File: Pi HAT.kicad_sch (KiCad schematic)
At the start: 13 parts, among them J1 Screw_Terminal_01x04, J2 Screw_Terminal_01x04, J3 Screw_Terminal_01x04, J5 Screw_Terminal_01x03, J6 Screw_Terminal_01x03, J7 GPIO_CONNECTOR, Q1 S8550

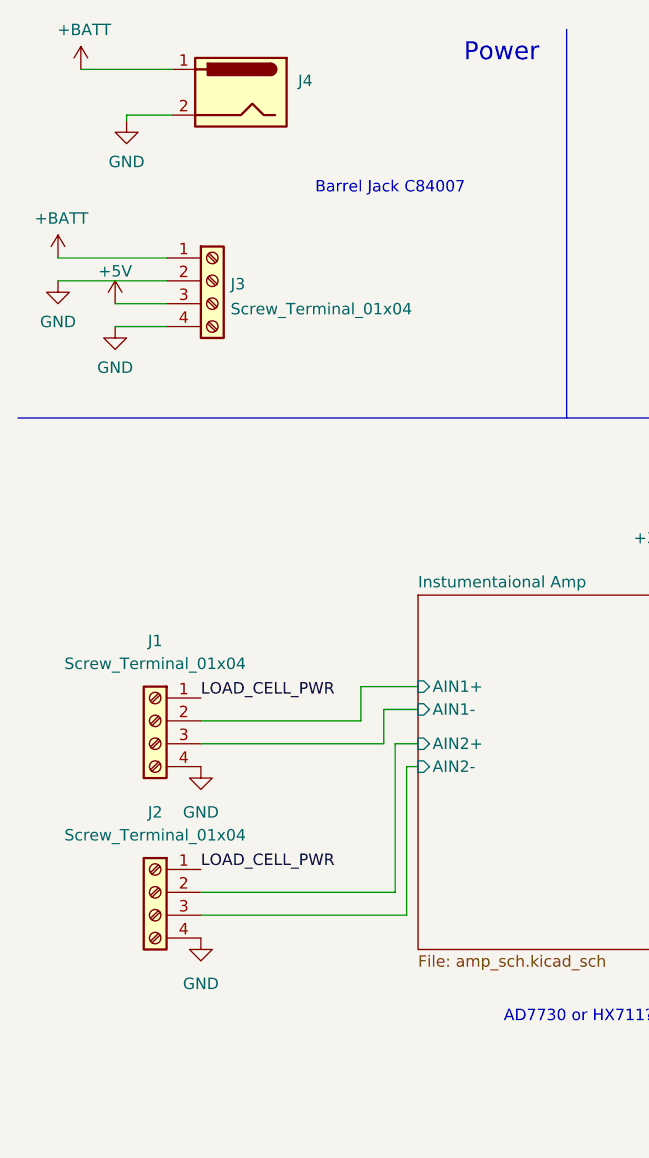
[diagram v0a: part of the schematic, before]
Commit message: Footprint assignment
Footprints yet to be assigned:
-U1: 74LVC125APW
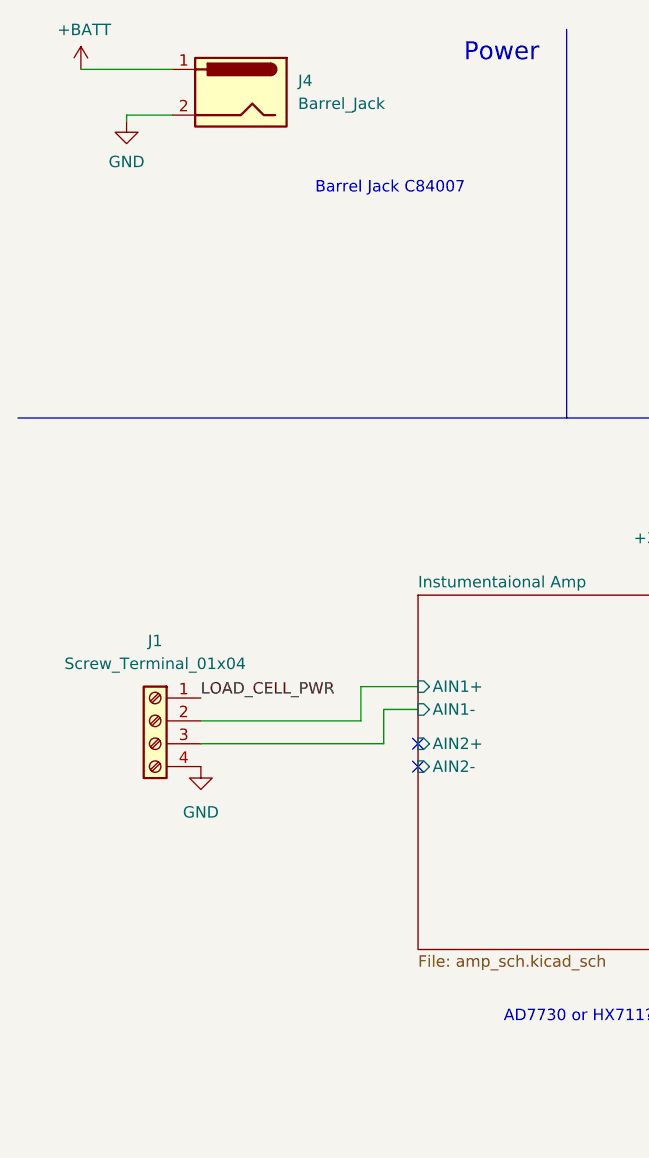
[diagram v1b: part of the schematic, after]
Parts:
- removed J2, J3: Screw_Terminal_01x04, symbol Connector:Screw_Terminal_01x04
- J1: footprint (none) -> TerminalBlock_4Ucon:TerminalBlock_4Ucon_1x04_P3.50mm_Vertical
- J4: value (none) -> Barrel_Jack; footprint (none) -> UCT:Barrel_Jack_2A_C84007
- J5, J6: footprint (none) -> TerminalBlock_4Ucon:TerminalBlock_4Ucon_1x03_P3.50mm_Vertical
- Q1: footprint Package_TO_SOT_THT:TO-92_Inline -> Package_TO_SOT_SMD:SOT-23
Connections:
- no-connect marks 25 -> 27

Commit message: Buffer footprint added
-fault in footprint for pi headers and load cell headers
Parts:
- J1: footprint TerminalBlock_4Ucon:TerminalBlock_4Ucon_1x04_P3.50mm_Vertical -> TerminalBlock:TerminalBlock_bornier-4_P5.08mm
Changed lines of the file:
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@@
     (property "Reference" "J1" (id 0) (at 27.94 80.645 0))
     (property "Value" "Screw_Terminal_01x04" (id 1) (at 27.94 83.185 0))
-    (property "Footprint" "TerminalBlock_4Ucon:TerminalBlock_4Ucon_1x04_P3.50mm_Vertical" (id 2) (at 27.94 89.535 0)
+    (property "Footprint" "TerminalBlock:TerminalBlock_bornier-4_P5.08mm" (id 2) (at 27.94 89.535 0)
       (effects (font (size 1.27 1.27)) hide)
     )
@@
     )
     (path "/4971e12a-d07a-4b0a-8cfd-ea8bd16efa5a"
-      (reference "J1") (unit 1) (value "Screw_Terminal_01x04") (footprint "TerminalBlock_4Ucon:TerminalBlock_4Ucon_1x04_P3.50mm_Vertical")
+      (reference "J1") (unit 1) (value "Screw_Terminal_01x04") (footprint "TerminalBlock:TerminalBlock_bornier-4_P5.08mm")
     )
     (path "/e7b3f30c-87be-4739-88d3-b191cd762eab"
@@
     )
     (path "/5ec412a6-29a4-46a1-a19b-d00a58557335/efbe0f43-2997-43b2-b307-a9e0d23db53f"
-      (reference "U1") (unit 1) (value "74LVC125APW,118") (footprint "SOP65P640X110-14N")
+      (reference "U1") (unit 1) (value "74LVC125APW,118") (footprint "74LVC125APW_118:SOP65P640X110-14N")
     )
     (path "/715798e8-ada1-4b31-bdfe-4378c151d2b8/00000000-0000-0000-0000-0000601048ab"

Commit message: Component placement
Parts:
- J1: footprint TerminalBlock:TerminalBlock_bornier-4_P5.08mm -> TerminalBlock_4Ucon:TerminalBlock_4Ucon_1x04_P3.50mm_Vertical
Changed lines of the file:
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@@
     (property "Reference" "J1" (id 0) (at 27.94 80.645 0))
     (property "Value" "Screw_Terminal_01x04" (id 1) (at 27.94 83.185 0))
-    (property "Footprint" "TerminalBlock:TerminalBlock_bornier-4_P5.08mm" (id 2) (at 27.94 89.535 0)
+    (property "Footprint" "TerminalBlock_4Ucon:TerminalBlock_4Ucon_1x04_P3.50mm_Vertical" (id 2) (at 27.94 89.535 0)
       (effects (font (size 1.27 1.27)) hide)
     )
@@
     )
     (path "/715798e8-ada1-4b31-bdfe-4378c151d2b8/00000000-0000-0000-0000-0000600c8c7d"
-      (reference "C11") (unit 1) (value "1u") (footprint "Capacitor_SMD:C_0603_1608Metric")
+      (reference "C11") (unit 1) (value "1u") (footprint "Capacitor_SMD:C_0402_1005Metric")
     )
     (path "/715798e8-ada1-4b31-bdfe-4378c151d2b8/00000000-0000-0000-0000-0000600ca45f"
@@
     )
     (path "/4971e12a-d07a-4b0a-8cfd-ea8bd16efa5a"
-      (reference "J1") (unit 1) (value "Screw_Terminal_01x04") (footprint "TerminalBlock:TerminalBlock_bornier-4_P5.08mm")
+      (reference "J1") (unit 1) (value "Screw_Terminal_01x04") (footprint "TerminalBlock_4Ucon:TerminalBlock_4Ucon_1x04_P3.50mm_Vertical")
     )
     (path "/e7b3f30c-87be-4739-88d3-b191cd762eab"
@@
     )
     (path "/715798e8-ada1-4b31-bdfe-4378c151d2b8/00000000-0000-0000-0000-000060149cd0"
-      (reference "J11") (unit 1) (value "Conn_01x02_Male") (footprint "TerminalBlock:TerminalBlock_Altech_AK300-2_P5.00mm")
+      (reference "J11") (unit 1) (value "Conn_01x02_Male") (footprint "Connector_PinHeader_2.54mm:PinHeader_1x02_P2.54mm_Vertical")
     )
     (path "/d7c66af1-6c08-458e-8338-6725a48e4fd1/f89deedb-7b72-4123-a68d-30d62fbf81e4"

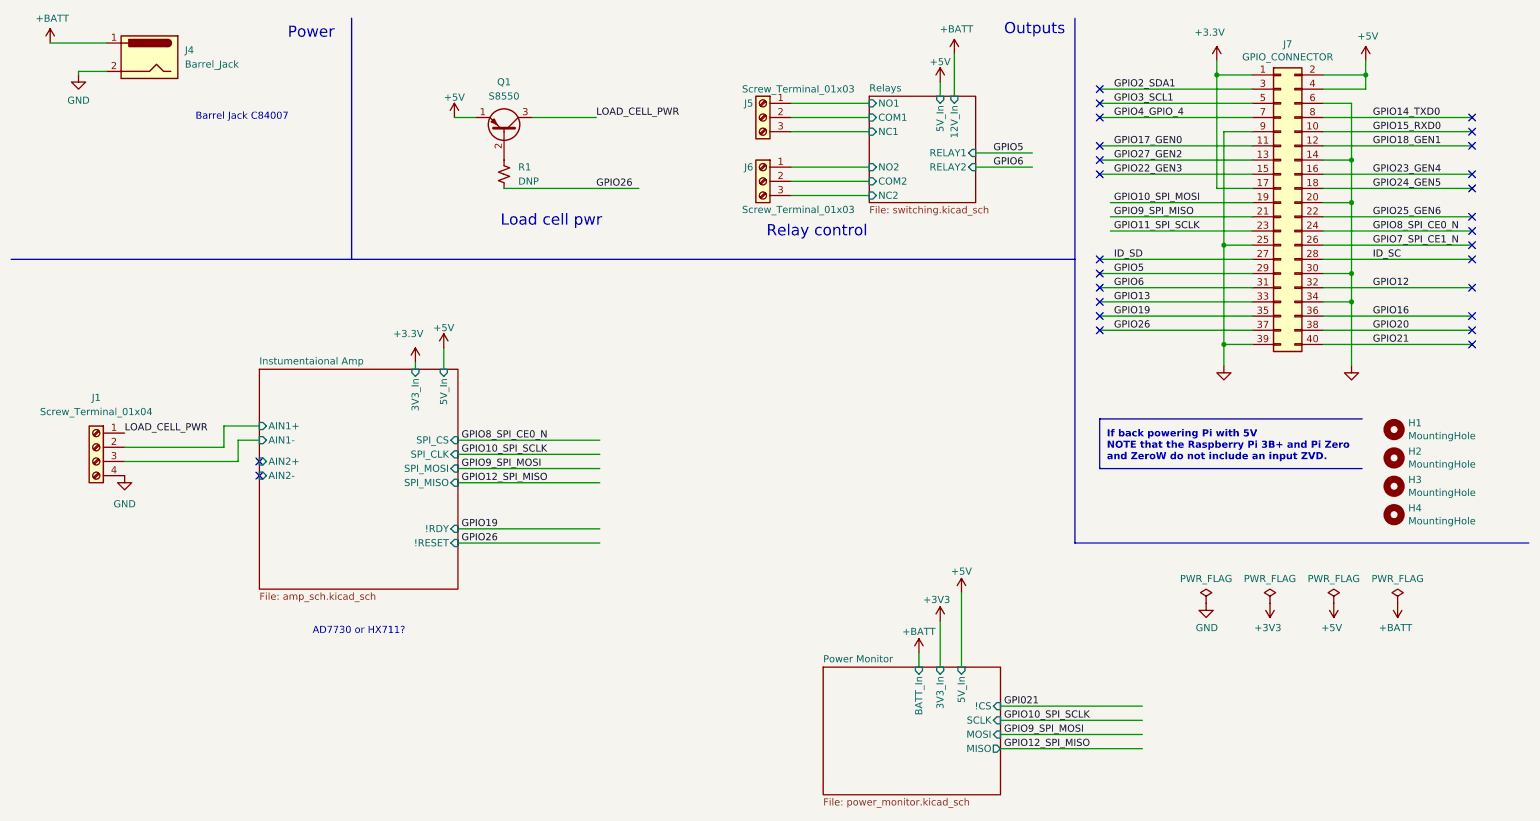
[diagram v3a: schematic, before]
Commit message: Reassigned pins to match placement
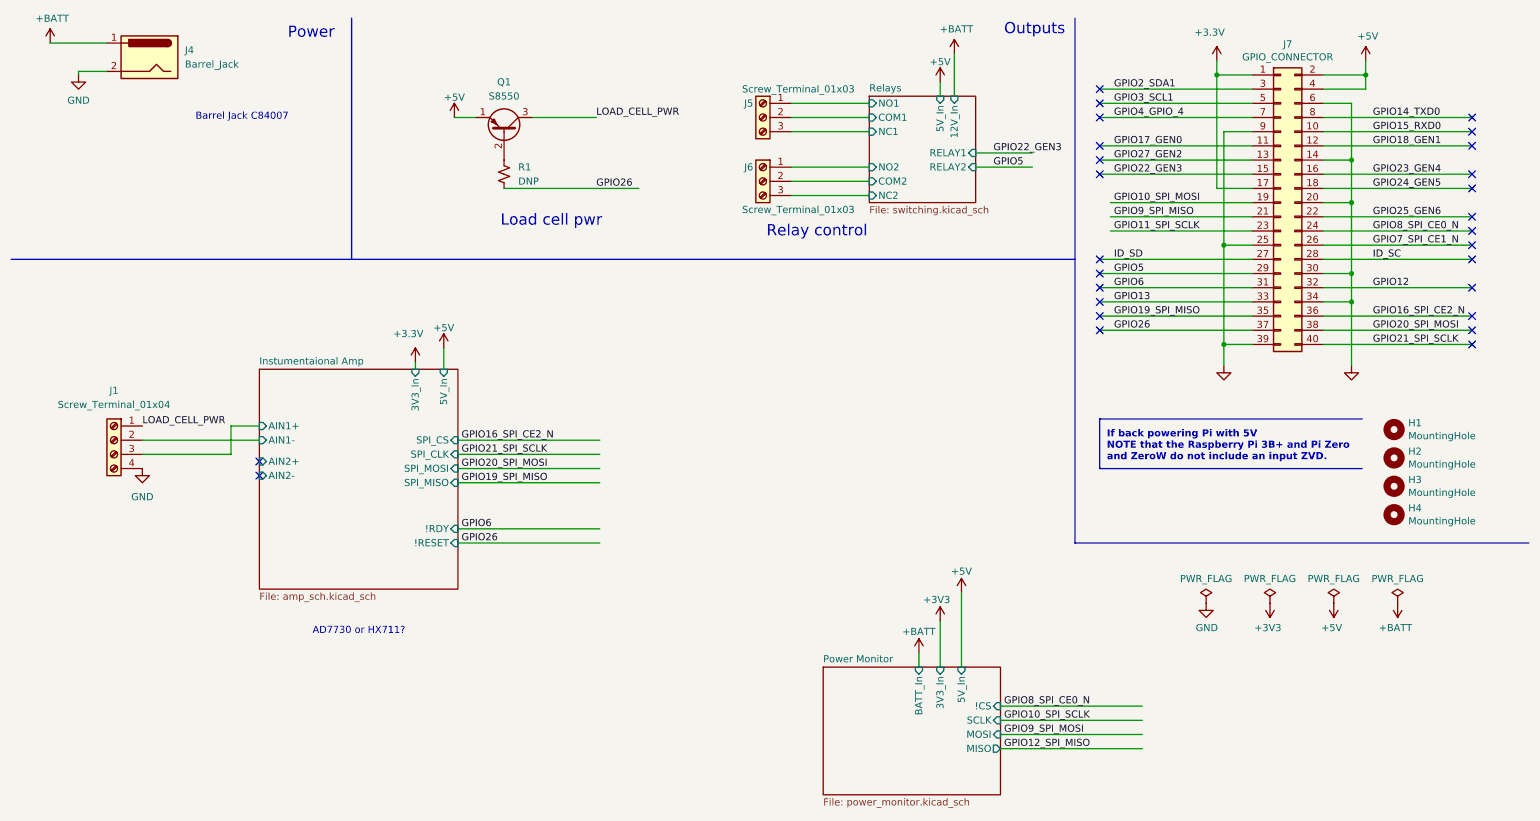
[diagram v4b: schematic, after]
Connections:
- net Instumentaional Amp/AIN1+: now also J1.3 (Pin_3); no longer J1.2 (Pin_2)
- net Instumentaional Amp/AIN1-: now also J1.2 (Pin_2); no longer J1.3 (Pin_3)
- net GPIO16 renamed GPIO16_SPI_CE2_N
- net GPIO19 renamed GPIO19_SPI_MISO
- net GPIO20 renamed GPIO20_SPI_MOSI
- net GPIO21 renamed GPIO21_SPI_SCLK
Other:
- moved on the sheet: J1
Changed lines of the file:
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@@
   (no_connect (at 274.32 53.34))
   (no_connect (at 207.645 66.04))
+  (wire (pts (xy 36.195 90.805) (xy 52.07 90.805))
+    (stroke (width 0) (type default) (color 0 0 0 0))
+  )
   (wire (pts (xy 152.4 27.94) (xy 166.37 27.94))
     (stroke (width 0) (type default) (color 0 0 0 0))
@@
     (stroke (width 0) (type default) (color 0 0 0 0))
   )
+  (wire (pts (xy 52.07 90.805) (xy 52.07 85.725))
+    (stroke (width 0) (type default) (color 0 0 0 0))
+  )
   (wire (pts (xy 247.65 30.48) (xy 274.32 30.48))
     (stroke (width 0) (type default) (color 0 0 0 0))
@@
     (stroke (width 0) (type default) (color 0 0 0 0))
   )
+  (wire (pts (xy 36.195 88.265) (xy 57.15 88.265))
+    (stroke (width 0) (type default) (color 0 0 0 0))
+  )
   (polyline (pts (xy 207.645 93.345) (xy 254.635 93.345))
     (stroke (width 0) (type default) (color 0 0 0 0))
@@
     (stroke (width 0) (type default) (color 0 0 0 0))
   )
-  (wire (pts (xy 53.34 92.075) (xy 53.34 88.265))
-    (stroke (width 0) (type default) (color 0 0 0 0))
-  )
   (wire (pts (xy 209.55 48.26) (xy 234.95 48.26))
     (stroke (width 0) (type default) (color 0 0 0 0))
@@
     (stroke (width 0) (type default) (color 0 0 0 0))
   )
-  (wire (pts (xy 33.02 92.075) (xy 53.34 92.075))
-    (stroke (width 0) (type default) (color 0 0 0 0))
-  )
   (wire (pts (xy 215.265 135.89) (xy 189.865 135.89))
     (stroke (width 0) (type default) (color 0 0 0 0))
@@
     (stroke (width 0) (type default) (color 0 0 0 0))
   )
-  (wire (pts (xy 50.8 85.725) (xy 57.15 85.725))
-    (stroke (width 0) (type default) (color 0 0 0 0))
-  )
   (polyline (pts (xy 284.48 106.68) (xy 203.2 106.68))
     (stroke (width 0) (type default) (color 0 0 0 0))
@@
     (stroke (width 0) (type default) (color 0 0 0 0))
   )
-  (wire (pts (xy 53.34 88.265) (xy 57.15 88.265))
-    (stroke (width 0) (type default) (color 0 0 0 0))
-  )
   (polyline (pts (xy 207.645 84.455) (xy 207.645 93.345))
     (stroke (width 0) (type default) (color 0 0 0 0))
   )
-  (wire (pts (xy 33.02 89.535) (xy 50.8 89.535))
-    (stroke (width 0) (type default) (color 0 0 0 0))
-  )
   (wire (pts (xy 152.4 39.37) (xy 166.37 39.37))
     (stroke (width 0) (type default) (color 0 0 0 0))
@@
     (stroke (width 0) (type default) (color 0 0 0 0))
   )
+  (wire (pts (xy 52.07 85.725) (xy 57.15 85.725))
+    (stroke (width 0) (type default) (color 0 0 0 0))
+  )
   (wire (pts (xy 92.71 88.265) (xy 118.11 88.265))
     (stroke (width 0) (type default) (color 0 0 0 0))
   )
   (wire (pts (xy 19.685 17.145) (xy 29.845 17.145))
-    (stroke (width 0) (type default) (color 0 0 0 0))
-  )
-  (wire (pts (xy 50.8 89.535) (xy 50.8 85.725))
     (stroke (width 0) (type default) (color 0 0 0 0))
   )
@@
     (effects (font (size 1.27 1.27)) (justify left bottom))
   )
-  (label "GPIO12_SPI_MISO" (at 93.345 95.885 0)
+  (label "GPIO19_SPI_MISO" (at 93.345 95.885 0)
     (effects (font (size 1.27 1.27)) (justify left bottom))
   )
@@
     (effects (font (size 1.27 1.27)) (justify left bottom))
   )
-  (label "GPIO21" (at 256.54 71.12 0)
-    (effects (font (size 1.27 1.27)) (justify left bottom))
-  )
-  (label "GPI021" (at 190.5 135.89 0)
-    (effects (font (size 1.27 1.27)) (justify left bottom))
-  )
-  (label "GPIO8_SPI_CE0_N" (at 93.345 88.265 0)
+  (label "GPIO21_SPI_SCLK" (at 256.54 71.12 0)
+    (effects (font (size 1.27 1.27)) (justify left bottom))
+  )
+  (label "GPIO8_SPI_CE0_N" (at 190.5 135.89 0)
+    (effects (font (size 1.27 1.27)) (justify left bottom))
+  )
+  (label "GPIO16_SPI_CE2_N" (at 93.345 88.265 0)
     (effects (font (size 1.27 1.27)) (justify left bottom))
   )
@@
     (effects (font (size 1.27 1.27)) (justify left bottom))
   )
-  (label "GPIO19" (at 93.345 104.14 0)
+  (label "GPIO6" (at 93.345 104.14 0)
     (effects (font (size 1.27 1.27)) (justify left bottom))
   )
@@
     (effects (font (size 1.27 1.27)) (justify left bottom))
   )
-  (label "GPIO9_SPI_MOSI" (at 93.345 93.345 0)
-    (effects (font (size 1.27 1.27)) (justify left bottom))
-  )
-  (label "GPIO20" (at 256.54 68.58 0)
-    (effects (font (size 1.27 1.27)) (justify left bottom))
-  )
-  (label "GPIO5" (at 188.595 36.83 0)
-    (effects (font (size 1.27 1.27)) (justify left bottom))
-  )
-  (label "GPIO19" (at 210.185 66.04 0)
-    (effects (font (size 1.27 1.27)) (justify left bottom))
-  )
-  (label "LOAD_CELL_PWR" (at 33.02 86.995 0)
-    (effects (font (size 1.27 1.27)) (justify left bottom))
-  )
-  (label "GPIO6" (at 188.595 39.37 0)
+  (label "GPIO20_SPI_MOSI" (at 93.345 93.345 0)
+    (effects (font (size 1.27 1.27)) (justify left bottom))
+  )
+  (label "GPIO20_SPI_MOSI" (at 256.54 68.58 0)
+    (effects (font (size 1.27 1.27)) (justify left bottom))
+  )
+  (label "GPIO22_GEN3" (at 188.595 36.83 0)
+    (effects (font (size 1.27 1.27)) (justify left bottom))
+  )
+  (label "GPIO19_SPI_MISO" (at 210.185 66.04 0)
+    (effects (font (size 1.27 1.27)) (justify left bottom))
+  )
+  (label "LOAD_CELL_PWR" (at 36.195 85.725 0)
+    (effects (font (size 1.27 1.27)) (justify left bottom))
+  )
+  (label "GPIO5" (at 188.595 39.37 0)
     (effects (font (size 1.27 1.27)) (justify left bottom))
   )
@@
     (effects (font (size 1.27 1.27)) (justify left bottom))
   )
-  (label "GPIO10_SPI_SCLK" (at 93.345 90.805 0)
+  (label "GPIO21_SPI_SCLK" (at 93.345 90.805 0)
     (effects (font (size 1.27 1.27)) (justify left bottom))
   )
@@
     (effects (font (size 1.27 1.27)) (justify left bottom))
   )
-  (label "GPIO16" (at 256.54 66.04 0)
+  (label "GPIO16_SPI_CE2_N" (at 256.54 66.04 0)
     (effects (font (size 1.27 1.27)) (justify left bottom))
   )
@@
     (pin "1")
   )
-  (symbol (lib_id "Connector:Screw_Terminal_01x04") (at 27.94 89.535 0) (mirror y) (unit 1)
+  (symbol (lib_id "Connector:Screw_Terminal_01x04") (at 31.115 88.265 0) (mirror y) (unit 1)
     (in_bom yes) (on_board yes) (fields_autoplaced)
-    (property "Reference" "J1" (id 0) (at 27.94 80.645 0))
-    (property "Value" "Screw_Terminal_01x04" (id 1) (at 27.94 83.185 0))
-    (property "Footprint" "TerminalBlock_4Ucon:TerminalBlock_4Ucon_1x04_P3.50mm_Vertical" (id 2) (at 27.94 89.535 0)
-      (effects (font (size 1.27 1.27)) hide)
-    )
-    (property "Datasheet" "~" (id 3) (at 27.94 89.535 0)
+    (property "Reference" "J1" (id 0) (at 31.115 79.375 0))
+    (property "Value" "Screw_Terminal_01x04" (id 1) (at 31.115 81.915 0))
+    (property "Footprint" "TerminalBlock_4Ucon:TerminalBlock_4Ucon_1x04_P3.50mm_Vertical" (id 2) (at 31.115 88.265 0)
+      (effects (font (size 1.27 1.27)) hide)
+    )
+    (property "Datasheet" "~" (id 3) (at 31.115 88.265 0)
       (effects (font (size 1.27 1.27)) hide)
     )
@@
     (pin "1")
   )
-  (symbol (lib_id "power:GND") (at 33.02 94.615 0) (unit 1)
+  (symbol (lib_id "power:GND") (at 36.195 93.345 0) (unit 1)
     (in_bom yes) (on_board yes) (fields_autoplaced)
-    (property "Reference" "#PWR07" (id 0) (at 33.02 100.965 0)
-      (effects (font (size 1.27 1.27)) hide)
-    )
-    (property "Value" "GND" (id 1) (at 33.02 99.695 0))
-    (property "Footprint" "" (id 2) (at 33.02 94.615 0)
-      (effects (font (size 1.27 1.27)) hide)
-    )
-    (property "Datasheet" "" (id 3) (at 33.02 94.615 0)
+    (property "Reference" "#PWR07" (id 0) (at 36.195 99.695 0)
+      (effects (font (size 1.27 1.27)) hide)
+    )
+    (property "Value" "GND" (id 1) (at 36.195 98.425 0))
+    (property "Footprint" "" (id 2) (at 36.195 93.345 0)
+      (effects (font (size 1.27 1.27)) hide)
+    )
+    (property "Datasheet" "" (id 3) (at 36.195 93.345 0)
       (effects (font (size 1.27 1.27)) hide)
     )
@@
     )
     (path "/5ec412a6-29a4-46a1-a19b-d00a58557335/f393b850-4261-4537-976f-66e22ad6e38f"
-      (reference "IC1") (unit 1) (value "AD7730") (footprint "Package_SO:SOIC-14_3.9x8.7mm_P1.27mm")
+      (reference "IC1") (unit 1) (value "AD7730") (footprint "Package_SO:TSSOP-24_4.4x7.8mm_P0.65mm")
     )
     (path "/4971e12a-d07a-4b0a-8cfd-ea8bd16efa5a"
